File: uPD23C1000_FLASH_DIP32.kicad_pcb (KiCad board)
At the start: 2 copper layers, 16.4 x 39.3 mm, 8 parts, among them J1 uPD23C1000 / FLASH, U1 GLS29EE010 (TSOP), U2 SST39SF010 (TSOP), U3 SST39SF010 / GLS29EE010 (PLCC)

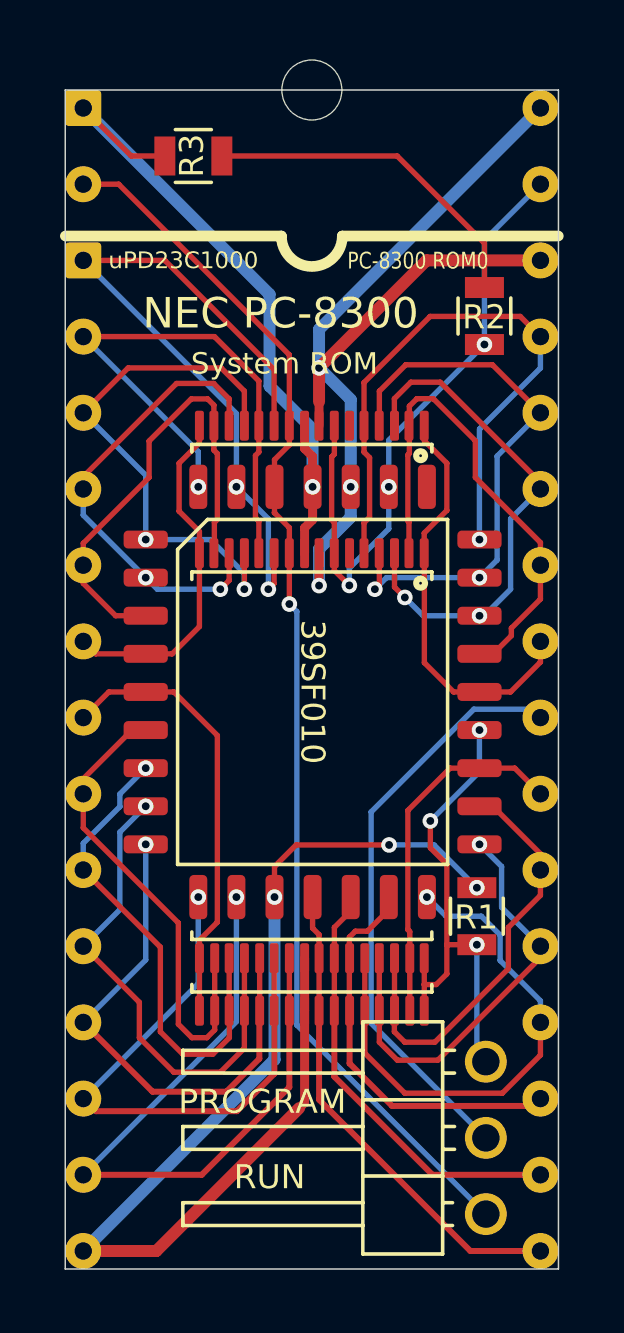
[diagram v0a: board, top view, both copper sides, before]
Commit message: FlashROM_8300: tsop footprints, zone fills
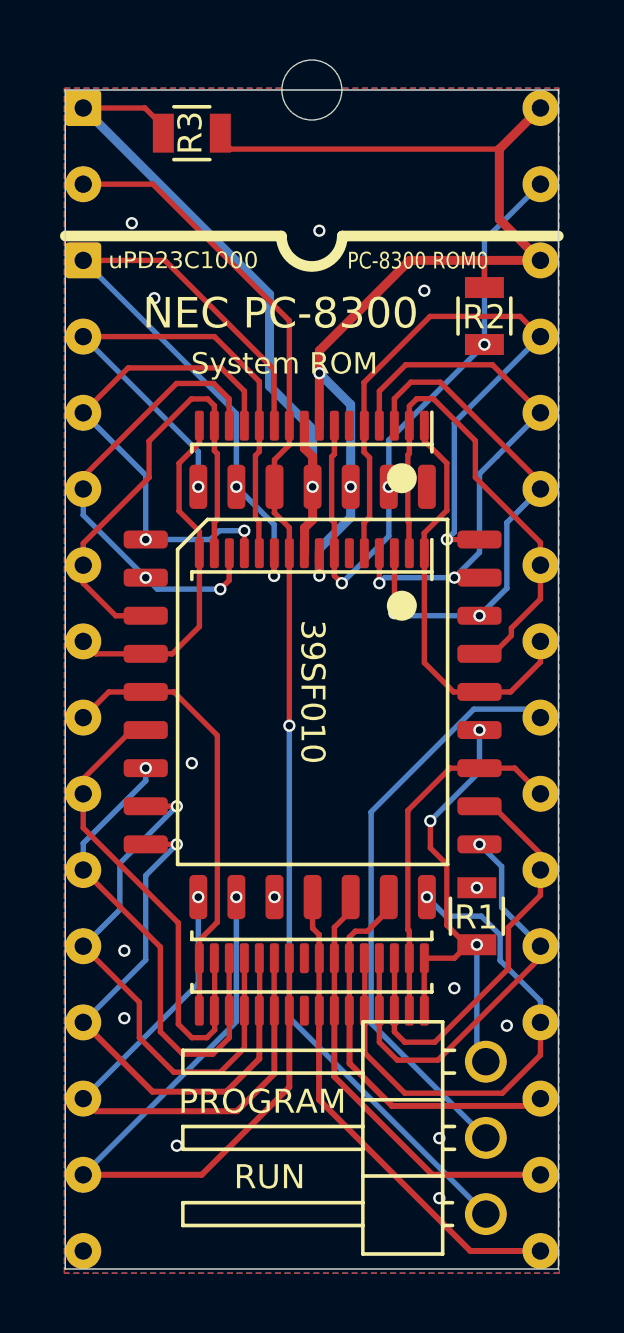
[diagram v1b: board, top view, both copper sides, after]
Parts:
- moved R3 0.76 mm to (146.0, 79.2)
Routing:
- net /GND: track 37.3 -> 0.00 mm, vias 3 -> 14
- net /VCC: track 43.2 -> 36.2 mm
- net /A14: track 20.5 -> 22.1 mm
- net /A7: track 18.1 -> 16.6 mm
- net /A0: track 16.7 -> 18.1 mm
- net /D0: track 17.4 -> 18.9 mm
- net /A15: track 24.5 -> 23.7 mm
- net /A16: track 41.0 -> 41.7 mm
- added copper zone on B.Cu, net /GND
- added copper zone on F.Cu, net /GND
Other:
- net class Default: clearance 0.2 -> 0.16; trace_width 0.25 -> 0.18; via_dia 0.8 -> 0.41; via_drill 0.4 -> 0.25
- rule trace_clearance: 0.2 -> 0.16
- rule via_min_drill: 0.26 -> 0.25
- rule via_min_size: 0.52 -> 0.41

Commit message: FlexROM_100 programming adapter, FlexROM_102 programming jumpers
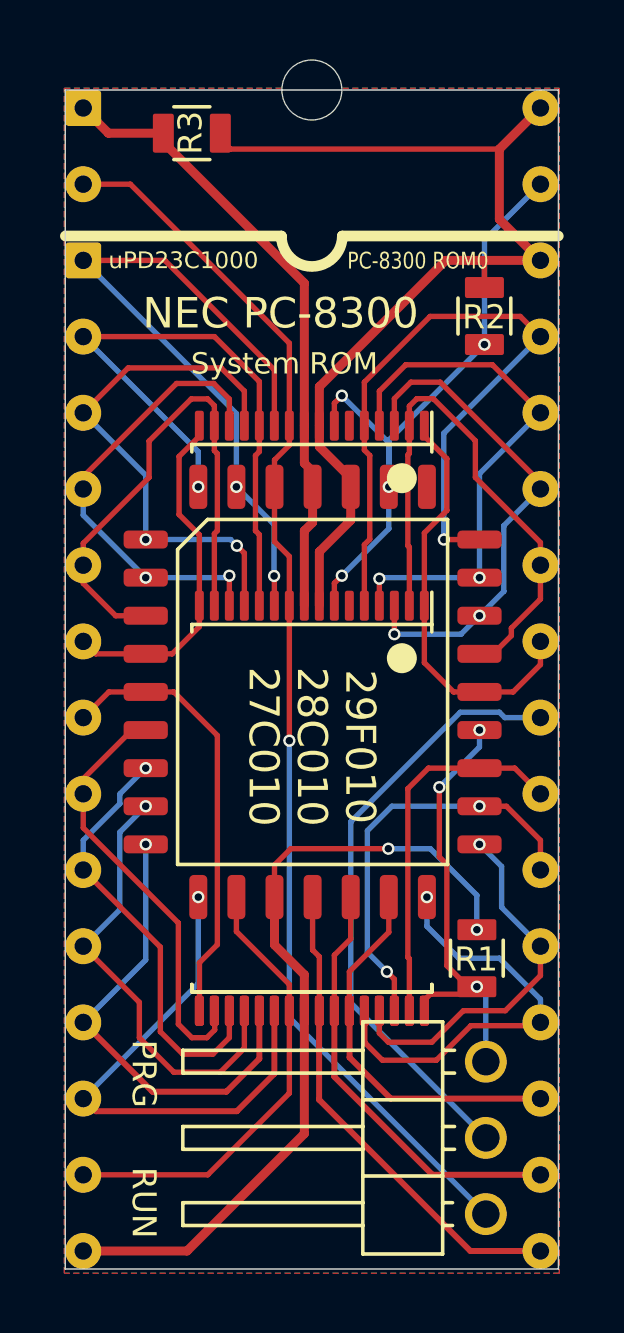
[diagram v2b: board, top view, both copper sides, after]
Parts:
- JP1: footprint 000_LOCAL:Pin_Header_Angled_1x03_Pitch2.54mm -> 000_LOCAL:Pin_Header_Angled_1x03_Pitch2.54mm_12shorted
- moved U2 1.75 mm to (150.0, 101.8)
- moved R1 1.40 mm to (155.5, 106.8)
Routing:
- net /GND: track 0.00 -> 27.1 mm, vias 14 -> 2
- net /D2: track 23.8 -> 15.3 mm, vias 1 -> 0
- net /D6: track 17.8 -> 14.4 mm
- net /A0: track 18.1 -> 14.9 mm
- net /D0: track 18.9 -> 15.7 mm
- net /VPP: track 23.4 -> 20.9 mm, vias 1 -> 0
- net /VCC: track 36.2 -> 34.0 mm, vias 3 -> 0
- net /D7: track 14.5 -> 12.4 mm
- net /A14: track 22.1 -> 23.9 mm
- net /A5: track 15.9 -> 17.8 mm
- net /A12: track 18.8 -> 20.7 mm
- net /A9: track 16.9 -> 18.7 mm
- net /D1: track 19.2 -> 17.5 mm
- net /A1: track 16.2 -> 14.5 mm
- net /A2: track 16.1 -> 14.4 mm
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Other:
- board text added: "29F010 28C010 27C010"
- board text added: "Move the jumper from RUN to PRG"
- board text added: "PRG"
- board text added: "To program:"
- board text removed: "39SF010"
- board text removed: "Configure programmer for PLCC version of chip (even if chip is TSOP)"
- board text removed: "Move the jumper from RUN to PROGRAM"
- board text removed: "PROGRAM"
- board text removed: "To program the flash chip:"
